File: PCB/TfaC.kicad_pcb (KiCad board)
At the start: 2 copper layers, 105 x 54 mm, 59 parts, among them IC501 ATMEGA88-A, M301 DisplayModule, P101 Line, P501 PRG, Q401 IRLML2502, Q402 IRLML2502, Q403 IRLML2502, Q404 IRLML2502, Q405 IRLML2502, Q406 IRLML2502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

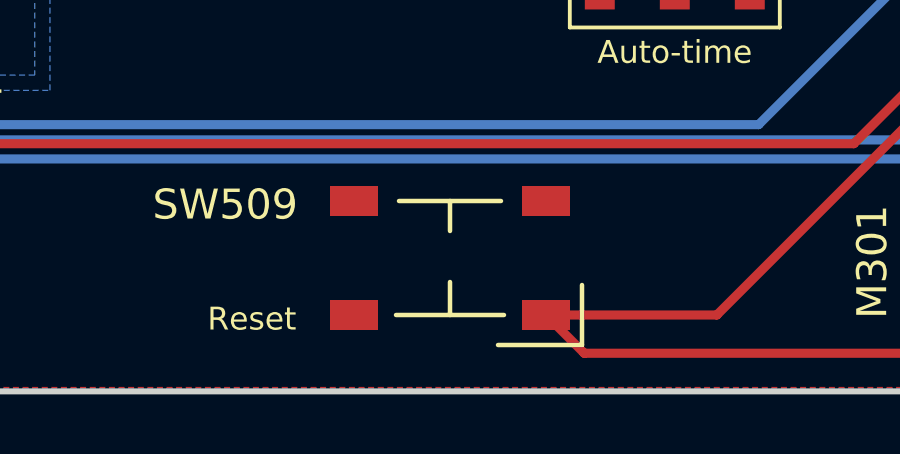
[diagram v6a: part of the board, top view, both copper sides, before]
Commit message: Added the missing track for the reset switch with the new foot print
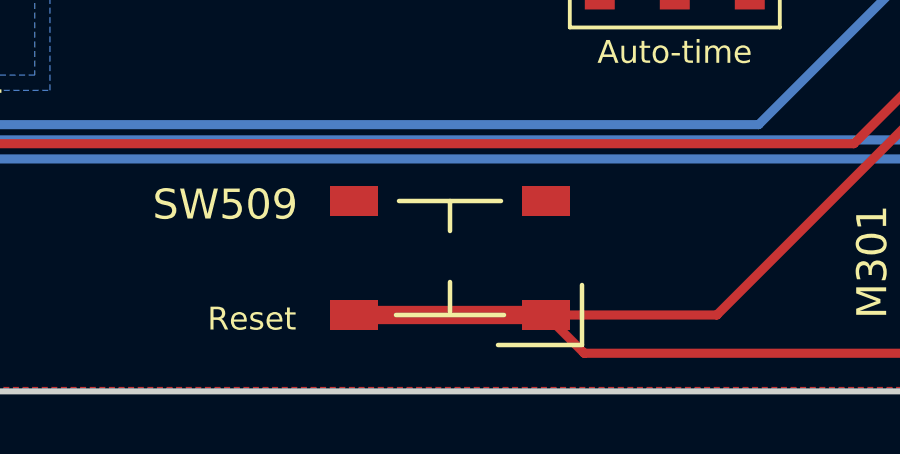
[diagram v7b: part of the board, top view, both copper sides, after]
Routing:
- net /Controller/Reset: track 84.8 -> 91.2 mm
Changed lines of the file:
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@@
-(kicad_pcb (version 4) (host pcbnew 4.0.0-stable)
+(kicad_pcb (version 4) (host pcbnew 4.0.1-2.201512121406+6195~38~ubuntu14.04.1-stable)
   (general
     (links 154)
-    (no_connects 1)
-    (area 96.399999 64.899999 201.600001 119.100001)
+    (no_connects 0)
+    (area 94.440438 63.8107 201.600001 120.920762)
     (thickness 1.6)
     (drawings 64)
-    (tracks 457)
+    (tracks 458)
     (zones 0)
     (modules 59)
@@
   )
   (setup
-    (last_trace_width 0.1524)
+    (last_trace_width 0.6096)
     (user_trace_width 0.3048)
     (user_trace_width 0.6096)
@@
   (segment (start 176.149 101.63302) (end 174.19702 101.63302) (width 0.6096) (layer F.Cu) (net 34))
   (segment (start 174.19702 101.63302) (end 173.99 101.426) (width 0.6096) (layer F.Cu) (net 34))
+  (segment (start 159.791 116.454) (end 153.391 116.454) (width 0.6096) (layer F.Cu) (net 35) (status C00000))
   (segment (start 159.791 116.454) (end 165.486 116.454) (width 0.3048) (layer F.Cu) (net 35))
   (segment (start 174.625 107.315) (end 175.895 107.315) (width 0.3048) (layer F.Cu) (net 35))

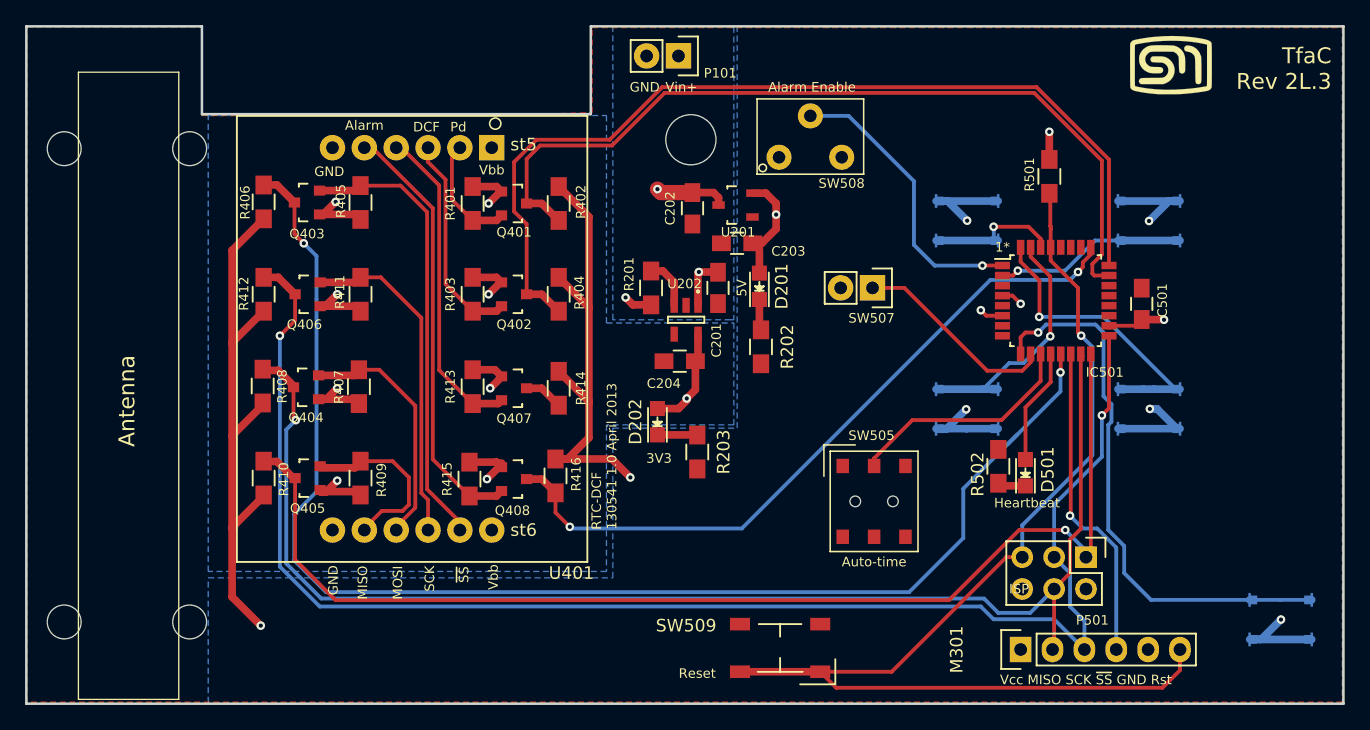
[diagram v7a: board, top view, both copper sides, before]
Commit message: Updated the routing to comply with the display module
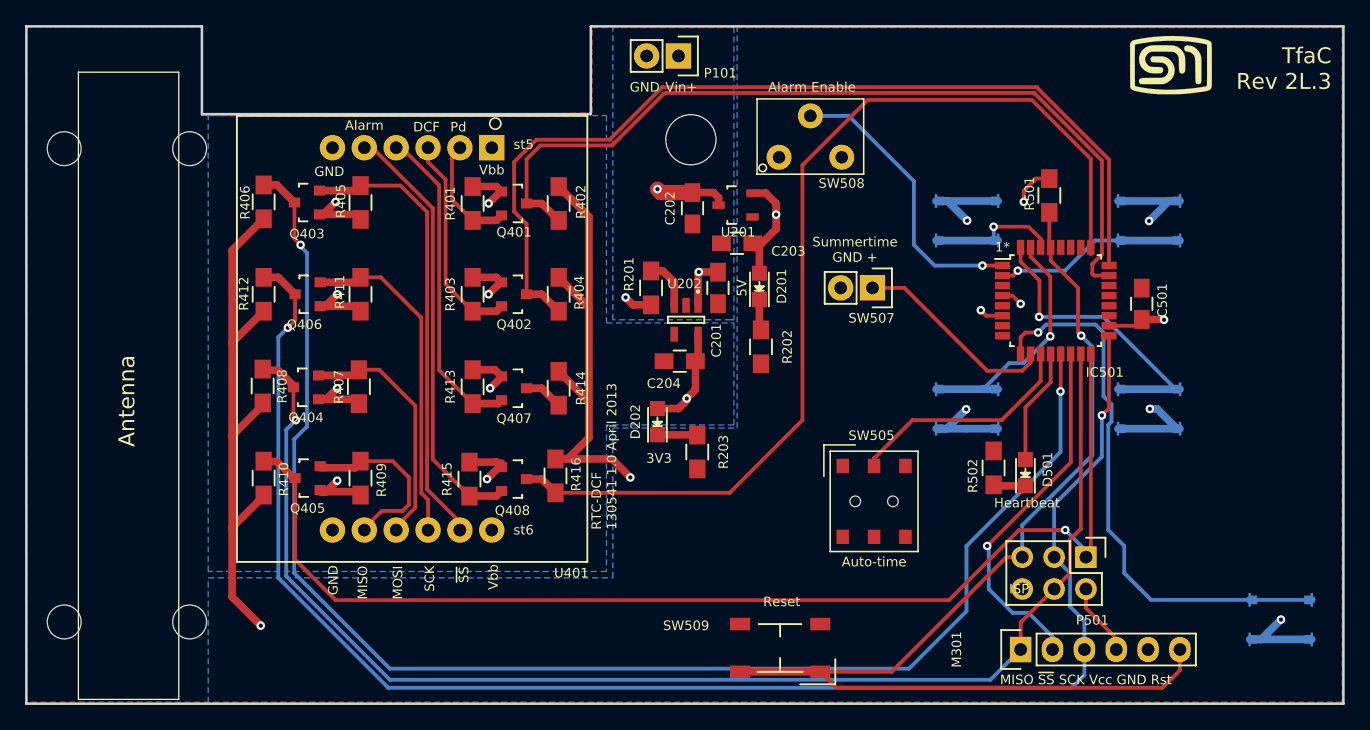
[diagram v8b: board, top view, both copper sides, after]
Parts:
- moved R501 1.52 mm to (178.1, 78.5)
- moved R502 0.40 mm to (173.6, 100.2)
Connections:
- IC501 pad 19: (no net) -> Net-(IC501-Pad19)
- IC501 pad 2: Alarm_Set -> Fast
- IC501 pad 20: (no net) -> Net-(IC501-Pad20)
- IC501 pad 22: (no net) -> Net-(IC501-Pad22)
- IC501 pad 26: (no net) -> Net-(IC501-Pad26)
- IC501 pad 27: (no net) -> Net-(IC501-Pad27)
- IC501 pad 28: (no net) -> Net-(IC501-Pad28)
- IC501 pad 31: Fast -> Alarm_Set
- IC501 pad 7: (no net) -> Net-(IC501-Pad7)
- IC501 pad 8: (no net) -> Net-(IC501-Pad8)
- M301 pad 1: /Controller/Vcc -> /Controller/MOSI
- M301 pad 2: /Controller/MOSI -> /Controller/~DISPLAY_SELECT
- M301 pad 4: /Controller/~DISPLAY_SELECT -> /Controller/Vcc
- SW502 pad 1: Alarm_Set -> Fast
- SW502 pad 2: Alarm_Set -> Fast
- SW503 pad 1: Fast -> Alarm_Set
- SW503 pad 2: Fast -> Alarm_Set
- SW505 pad 1: (no net) -> Net-(SW505-Pad1)
- SW508 pad 1: (no net) -> Net-(SW508-Pad1)
- U202 pad 4: (no net) -> Net-(U202-Pad4)
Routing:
- net /Controller/ALARM_INT: track 57.4 -> 79.9 mm, vias 2 -> 0
- net /Controller/~RTC_SELECT: track 108.2 -> 115.7 mm
- net /Controller/Vcc: track 102.9 -> 110.2 mm
- net /Controller/SCK: track 121.1 -> 125.5 mm
- net Fast: track 19.8 -> 15.6 mm
- net Alarm_Set: track 15.6 -> 19.8 mm
- net /Controller/~DISPLAY_SELECT: track 26.1 -> 29.4 mm
- net /Controller/Reset: track 91.2 -> 89.1 mm
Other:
- board text added: "MISO ~SS~ SCK Vcc GND Rst"
- board text added: "Summertime GND +"
- board text removed: "Vcc MISO SCK ~SS~ GND Rst"
